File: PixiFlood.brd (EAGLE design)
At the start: 55.9 x 45.7 mm, 62 parts, among them IC1 L78LXXCU/BU, IC2 74LVC1G125DBV, IC3 LM1117-SOT223, IC4 WS2811SOP8, IC5 TC7W04FP-0.65, U1 PT4115B89E, U2 PT4115B89E, U3 PT4115B89E, X1 22-23-2041

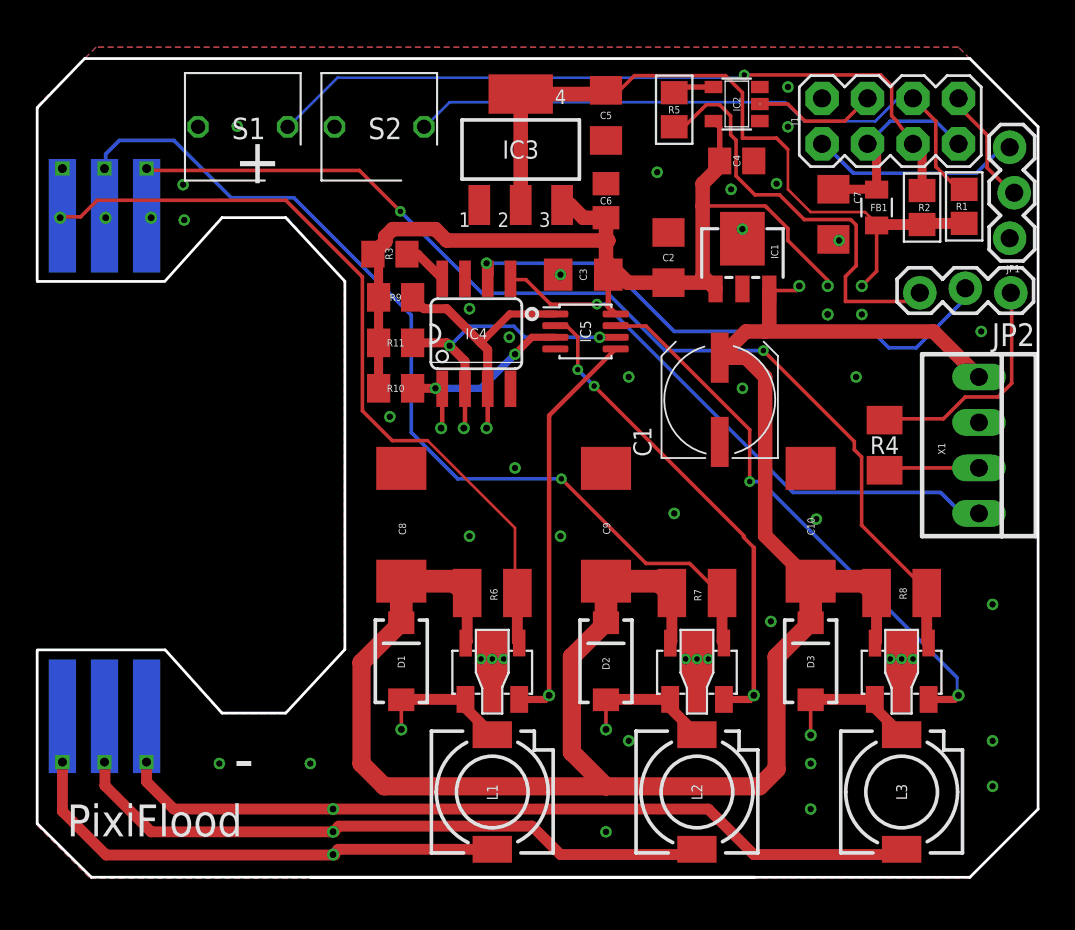
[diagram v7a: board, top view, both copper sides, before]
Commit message: Reworked layout
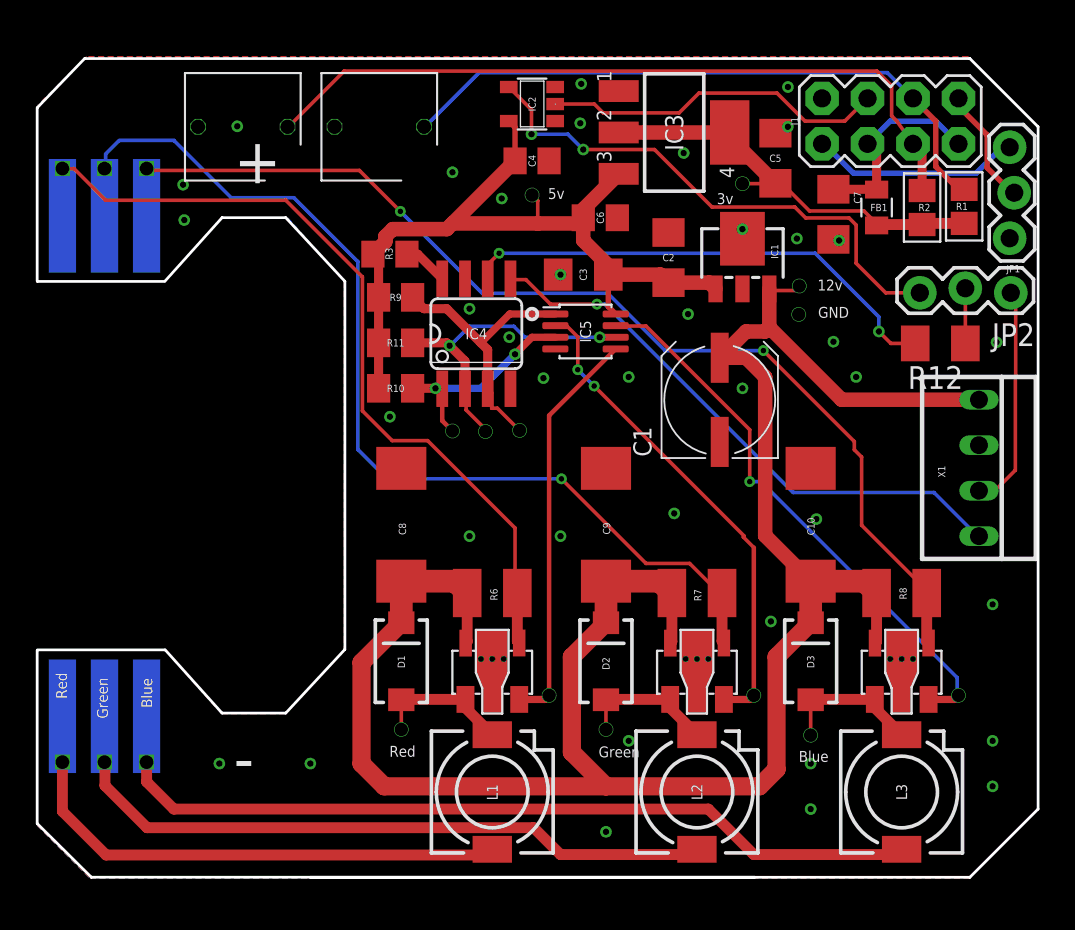
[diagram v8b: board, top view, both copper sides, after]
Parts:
- removed R4: 33R, rcl:M1206
- removed R5: 100, resistors:R0805
- removed TP26, TP27, TP28, TP29, TP30, TP31: TEST-POINTTP_15TH_THRU, SparkFun-Connectors:TP_15TH
- added R12: 33R, rcl:M1206
- TP1, TP10, TP17, TP18, TP19, TP2, TP20, TP21, TP22, TP23, TP24, TP25, TP3: value TEST-POINTTP_15TH_THRU -> TEST_PINTP-1; device SparkFun-Connectors:TP_15TH -> connectors:TP-1
- moved TP10 17.3 mm to (27.6, 38.1)
- moved C4 11.4 mm to (27.6, 40.0)
- moved IC2 11.4 mm to (27.6, 43.2)
- moved C5 9.76 mm to (41.2, 40.2), turned to 90 degrees
- moved TP19 8.78 mm to (39.4, 38.7)
- moved IC3 8.63 mm to (35.6, 41.6), turned to 270 degrees
- moved TP21 1.85 mm to (26.9, 25.0)
- moved TP18 1.62 mm to (42.5, 31.4)
- moved X1 1.27 mm to (52.6, 22.9)
- moved TP22 1.22 mm to (25.0, 24.9)
- moved C6 1.00 mm to (31.4, 36.8), turned to 0 degrees
- moved TP24 0.65 mm to (23.2, 24.9)
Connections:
- removed net DIN-W: R4.1, X1.3
- removed net N$6: IC2.4, R5.2
- new net N$7: JP2.2, R12.1
- net BOUT: no longer TP30.P$1
- net DIN: now also R12.2; no longer JP2.2
- net GOUT: no longer TP29.P$1
- net LED-B-NEG: no longer TP31.P$1
- net LED-G-NEG: no longer TP28.P$1
- net LED-R-NEG: no longer TP27.P$1
- net ROUT: no longer TP26.P$1
- net WIFI: now also IC2.4; no longer R5.1
- net WIRED: now also X1.3; no longer R4.2
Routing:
- net +3V3: track 41.4 -> 23.5 mm
- net GPIO2: track 6.93 -> 19.3 mm
- net +5V: track 57.2 -> 45.1 mm
- net WIFI: track 24.1 -> 29.8 mm, vias 0 -> 2
- net DIN-W: track 5.34 -> 0.00 mm
- net DIN: track 31.7 -> 27.5 mm, vias 1 -> 2
- net N$7: track 0.00 -> 3.08 mm
- net N$6: track 2.32 -> 0.00 mm
- net GOUT: track 55.4 -> 57.6 mm
- net N$16: track 14.6 -> 15.7 mm
- net N$4: track 17.1 -> 17.7 mm
- net LED-G-NEG: track 39.3 -> 38.8 mm
- net RST: track 41.6 -> 41.8 mm, vias 1 -> 0
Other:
- board text added: "12v"
- board text added: "3v"
- board text added: "5v"
- board text added: "Blue"
- board text added: "GND"
- board text added: "Green"
- board text added: "Red"
- board text added: "V1.5"
- board text removed: "V1.2w"
